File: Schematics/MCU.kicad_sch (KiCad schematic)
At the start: 17 parts, among them SW1 SW_Push, SW2 SW_Push, U1 STM32F405RGTx

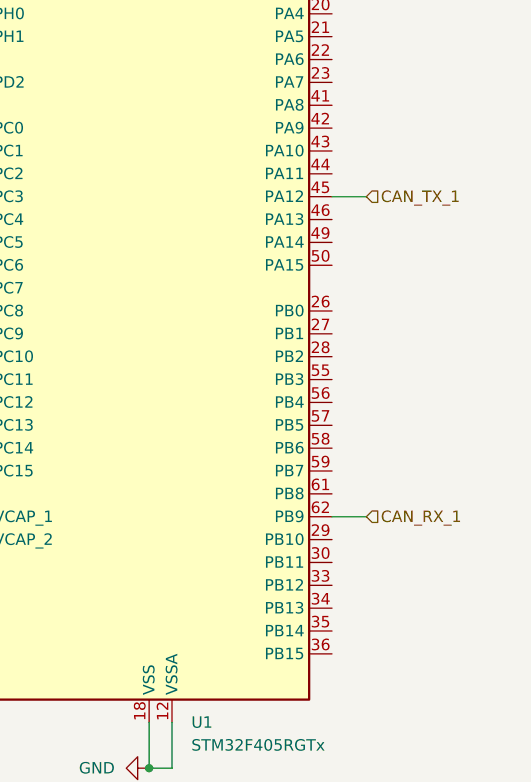
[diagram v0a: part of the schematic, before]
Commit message: added usb type C and changed to CAN2
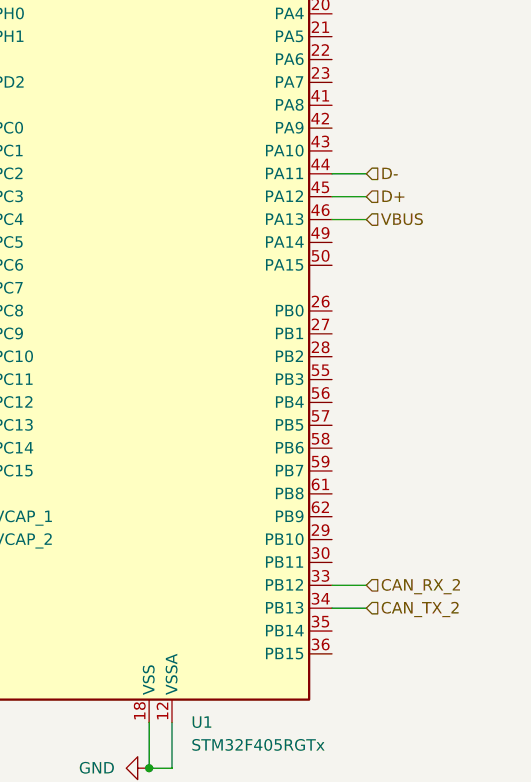
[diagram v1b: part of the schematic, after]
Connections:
- net CAN_RX_2: now reaches U1.33 (PB12)
- net CAN_TX_2: now reaches U1.34 (PB13)
- net D-: now reaches U1.44 (PA11)
- net VBUS: now reaches U1.46 (PA13)
- net CAN_RX_1: no longer names the net of U1.62 (PB9)
- net CAN_TX_1 renamed D+
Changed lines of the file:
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@@
+	(wire
+		(pts
+			(xy 185.42 83.82) (xy 189.23 83.82)
+		)
+		(stroke
+			(width 0)
+			(type default)
+		)
+	)
 	(wire
 		(pts
@@
 	(wire
 		(pts
+			(xy 185.42 86.36) (xy 189.23 86.36)
+		)
+		(stroke
+			(width 0)
+			(type default)
+		)
+	)
+	(wire
+		(pts
+			(xy 185.42 127) (xy 189.23 127)
+		)
+		(stroke
+			(width 0)
+			(type default)
+		)
+	)
+	(wire
+		(pts
 			(xy 125.73 78.74) (xy 144.78 78.74)
 		)
@@
 	(wire
 		(pts
-			(xy 185.42 83.82) (xy 189.23 83.82)
+			(xy 185.42 81.28) (xy 189.23 81.28)
 		)
 		(stroke
@@
 	(wire
 		(pts
+			(xy 185.42 129.54) (xy 189.23 129.54)
+		)
+		(stroke
+			(width 0)
+			(type default)
+		)
+	)
+	(wire
+		(pts
 			(xy 167.64 147.32) (xy 167.64 142.24)
 		)
@@
 		(pts
 			(xy 115.57 30.48) (xy 119.38 30.48)
-		)
-		(stroke
-			(width 0)
-			(type default)
-		)
-	)
-	(wire
-		(pts
-			(xy 189.23 119.38) (xy 185.42 119.38)
 		)
 		(stroke
@@
 		)
 	)
-	(hierarchical_label "CAN_TX_1"
+	(hierarchical_label "CAN_TX_2"
+		(shape input)
+		(at 189.23 129.54 0)
+		(effects
+			(font
+				(size 1.27 1.27)
+			)
+			(justify left)
+		)
+	)
+	(hierarchical_label "UART_DEBUG_TX"
+		(shape input)
+		(at 140.97 106.68 180)
+		(effects
+			(font
+				(size 1.27 1.27)
+			)
+			(justify right)
+		)
+	)
+	(hierarchical_label "UART_DEBUG_RX"
+		(shape input)
+		(at 140.97 71.12 180)
+		(effects
+			(font
+				(size 1.27 1.27)
+			)
+			(justify right)
+		)
+	)
+	(hierarchical_label "CAN_RX_2"
+		(shape input)
+		(at 189.23 127 0)
+		(effects
+			(font
+				(size 1.27 1.27)
+			)
+			(justify left)
+		)
+	)
+	(hierarchical_label "CAM_L_PWN_EN"
+		(shape input)
+		(at 125.73 76.2 180)
+		(effects
+			(font
+				(size 1.27 1.27)
+			)
+			(justify right)
+		)
+	)
+	(hierarchical_label "VBUS"
+		(shape input)
+		(at 189.23 86.36 0)
+		(effects
+			(font
+				(size 1.27 1.27)
+			)
+			(justify left)
+		)
+	)
+	(hierarchical_label "D-"
+		(shape input)
+		(at 189.23 81.28 0)
+		(effects
+			(font
+				(size 1.27 1.27)
+			)
+			(justify left)
+		)
+	)
+	(hierarchical_label "D+"
 		(shape input)
 		(at 189.23 83.82 0)
@@
 		)
 	)
-	(hierarchical_label "UART_DEBUG_TX"
-		(shape input)
-		(at 140.97 106.68 180)
-		(effects
-			(font
-				(size 1.27 1.27)
-			)
-			(justify right)
-		)
-	)
-	(hierarchical_label "UART_DEBUG_RX"
-		(shape input)
-		(at 140.97 71.12 180)
-		(effects
-			(font
-				(size 1.27 1.27)
-			)
-			(justify right)
-		)
-	)
-	(hierarchical_label "CAN_RX_1"
-		(shape input)
-		(at 189.23 119.38 0)
-		(effects
-			(font
-				(size 1.27 1.27)
-			)
-			(justify left)
-		)
-	)
-	(hierarchical_label "CAM_L_PWN_EN"
-		(shape input)
-		(at 125.73 76.2 180)
-		(effects
-			(font
-				(size 1.27 1.27)
-			)
-			(justify right)
-		)
-	)

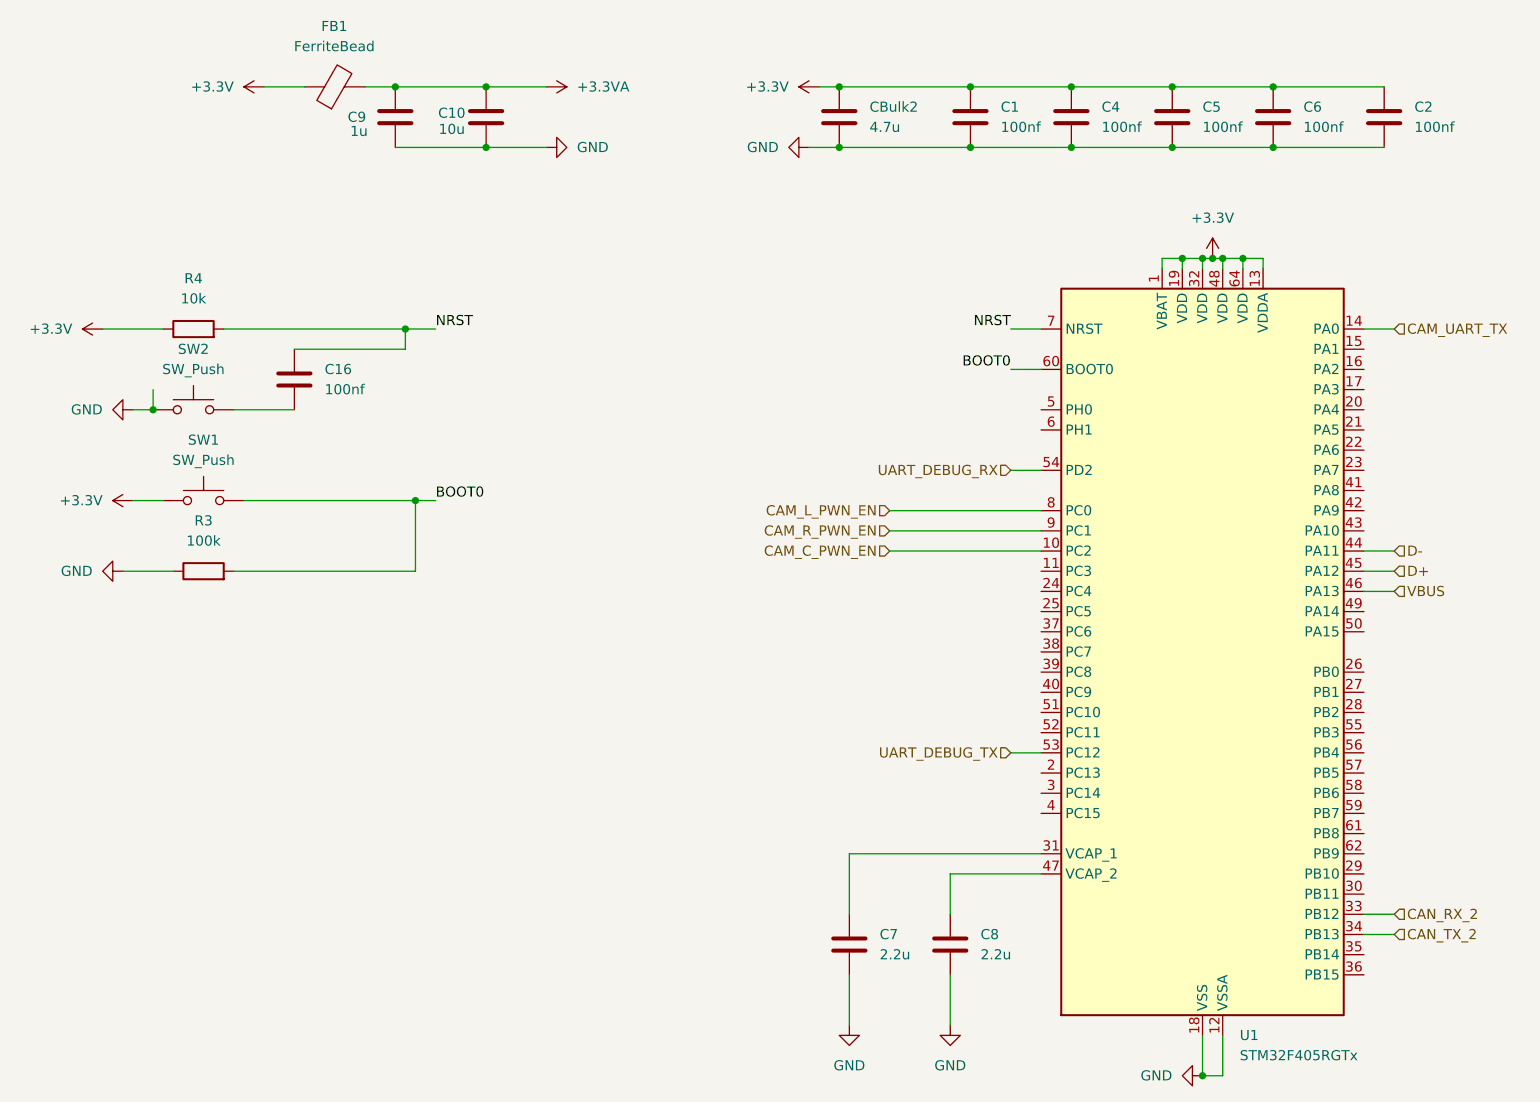
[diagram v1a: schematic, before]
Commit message: finished LED one Power and one Programable
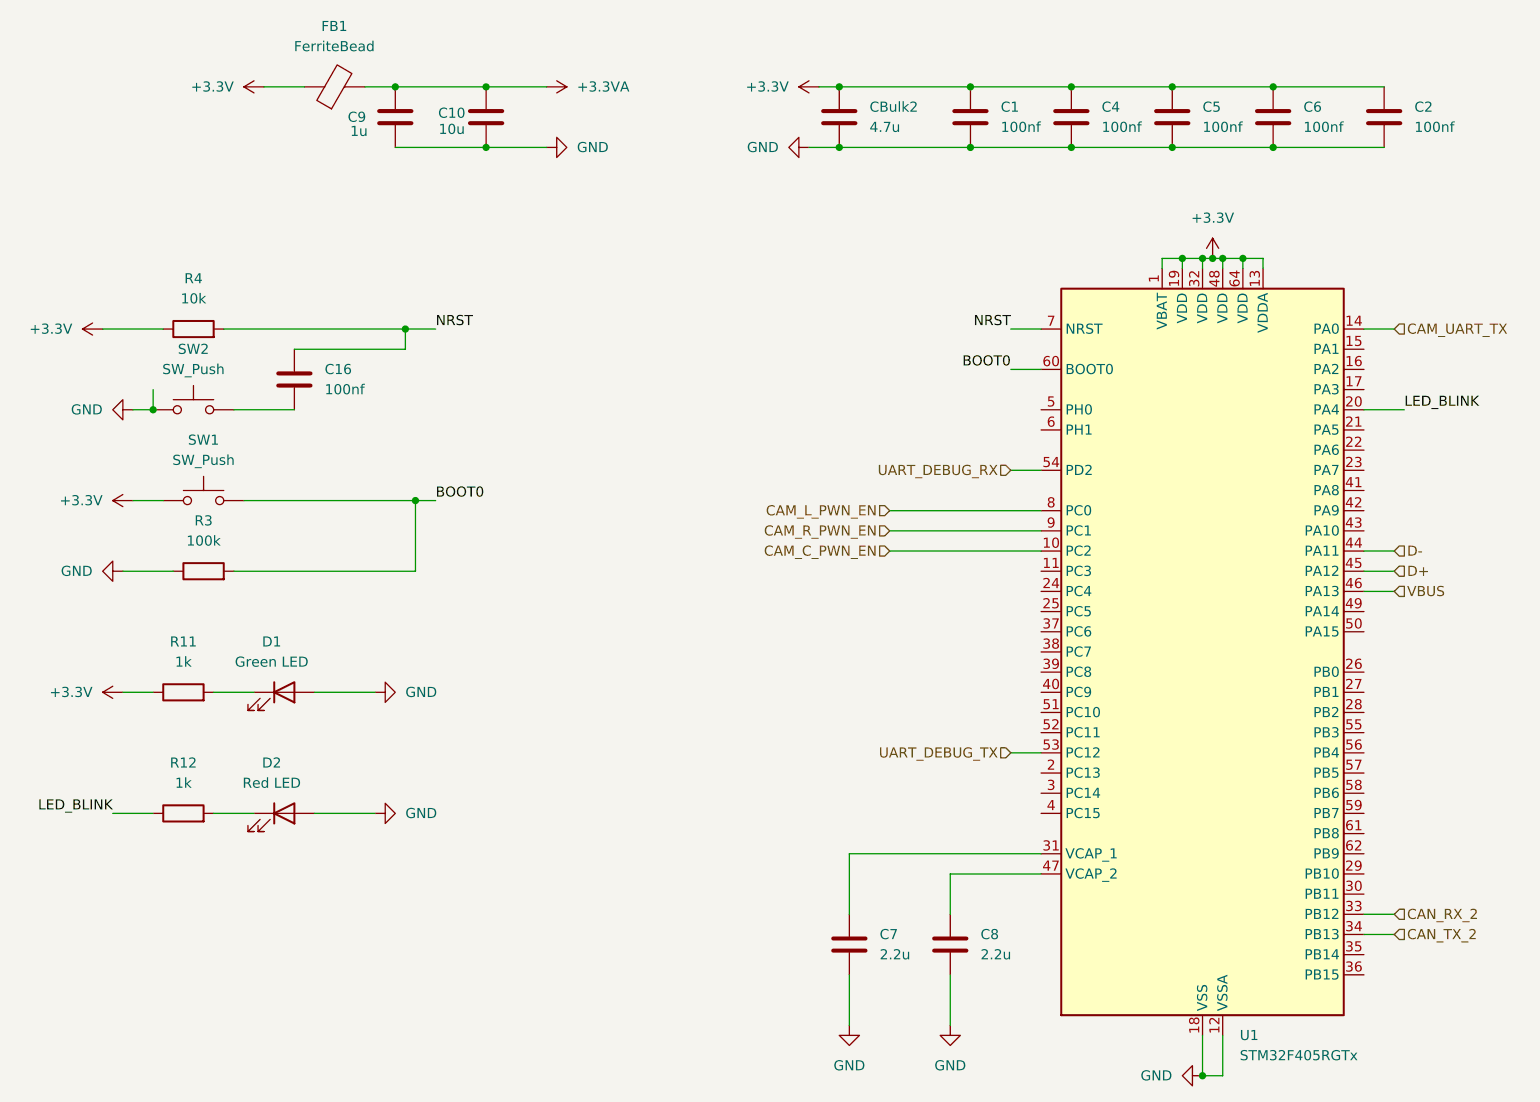
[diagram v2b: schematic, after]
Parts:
- added D1: Green LED, symbol Device:LED
- added D2: Red LED, symbol Device:LED
- added R11, R12: 1k, symbol Device:R
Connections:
- net +3.3V: now also R11.1
- net GND: now also D1.2 (A), D2.2 (A)
- net LED_BLINK: now reaches U1.20 (PA4)
- net LED_BLINK: now also R12.1
- new net: D2.1 (K), R12.2
- new net: D1.1 (K), R11.2

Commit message: assigned footprints ready for pcb design
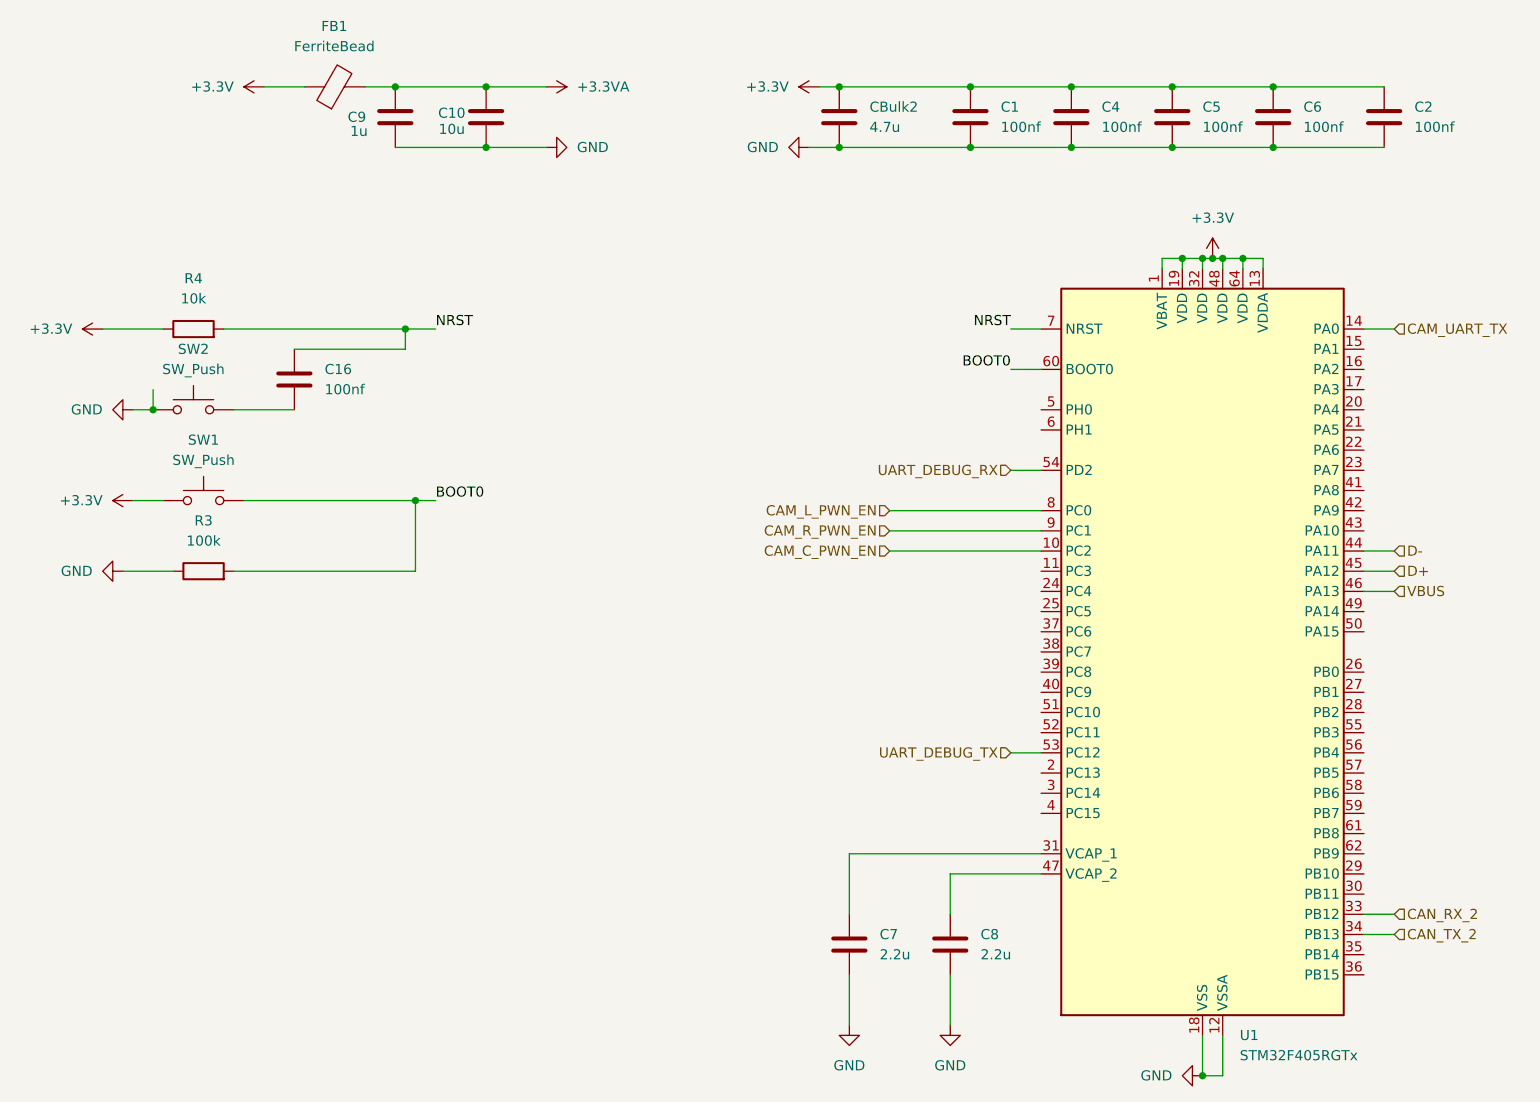
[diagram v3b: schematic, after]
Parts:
- removed D1: Green LED, symbol Device:LED
- removed D2: Red LED, symbol Device:LED
- removed R11, R12: 1k, symbol Device:R
- C1, C10, C16, C2, C4, C5, C6, C7, C8, C9, CBulk2: footprint (none) -> Capacitor_SMD:C_0805_2012Metric_Pad1.18x1.45mm_HandSolder
- FB1, R3, R4: footprint (none) -> Resistor_SMD:R_0805_2012Metric_Pad1.20x1.40mm_HandSolder
- SW1, SW2: footprint (none) -> Button_Switch_THT:SW_PUSH_1P1T_6x3.5mm_H5.0_APEM_MJTP1250
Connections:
- net LED_BLINK: no longer names the net of U1.20 (PA4)
